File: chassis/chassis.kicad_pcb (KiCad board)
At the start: 2 copper layers, 157.5 x 43.2 mm, 84 parts, among them J1 RJ45_LED_Shielded, Q1 SiR422DP, Q2 Si7898DP, Q3 MMDT3906, T1 PoE_Transformer, T2 Pulse_Transformer, U1 TPS23754PWPR, U2 TCMT1107, U3 TCMT1107, U4 KSZ8081RND, U5 L78L33_SO8, U6 EFM32GG11B8xx

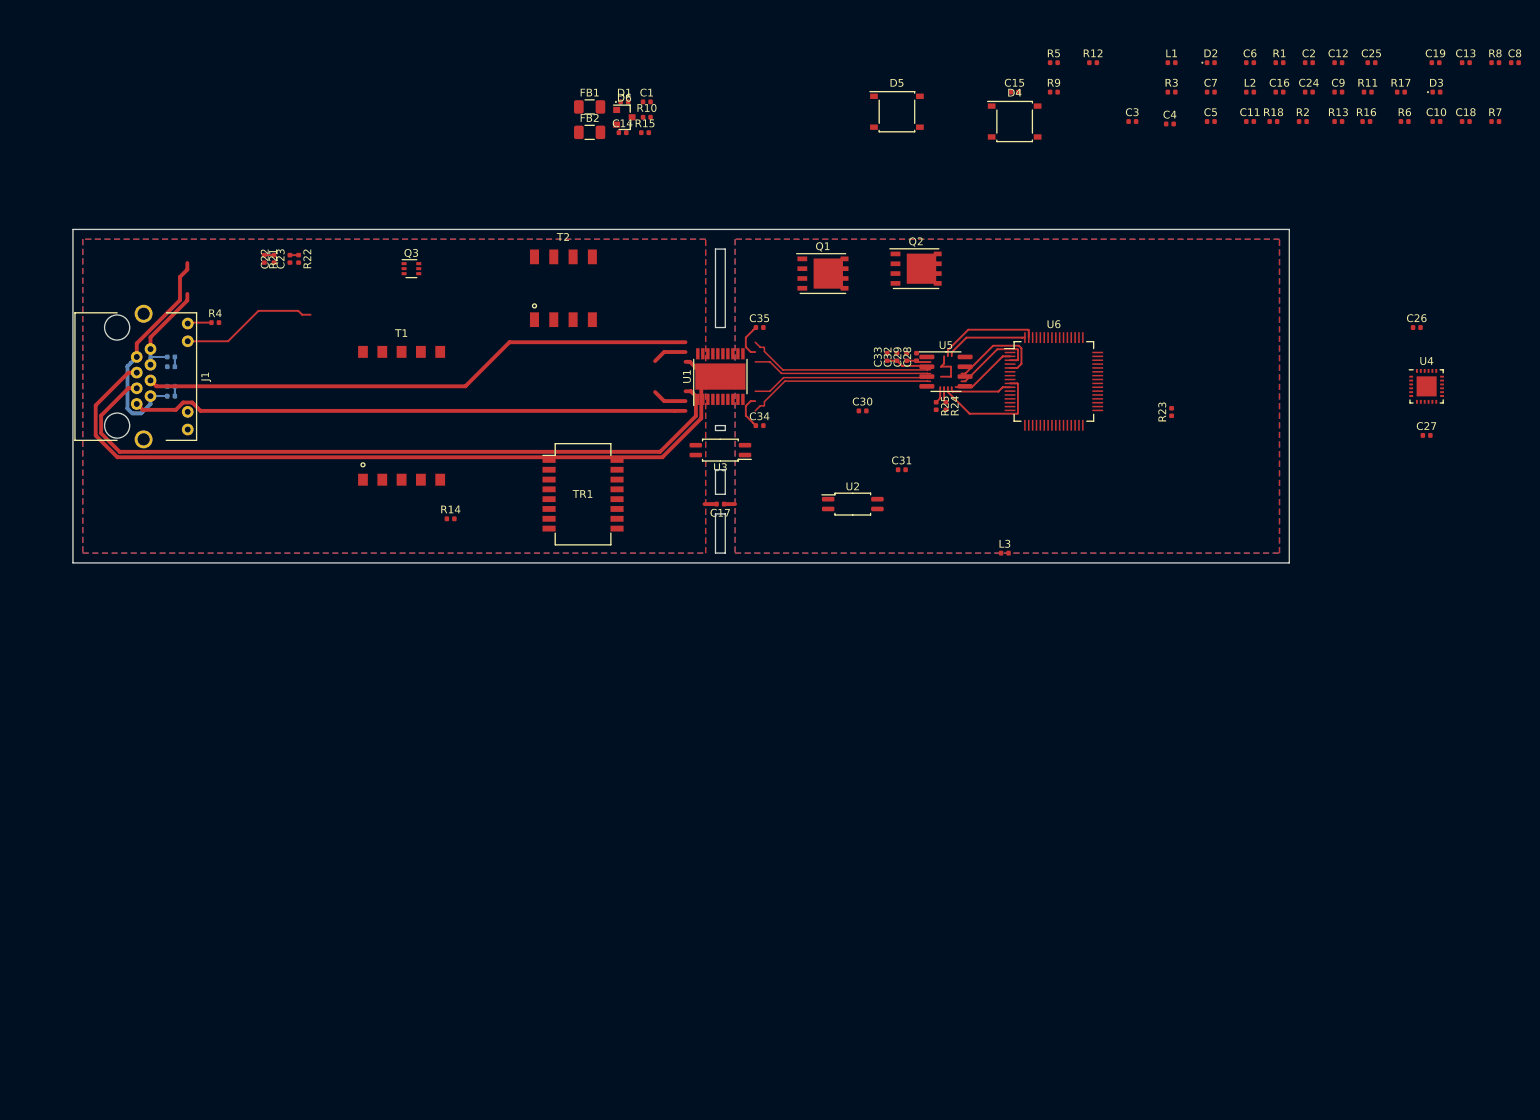
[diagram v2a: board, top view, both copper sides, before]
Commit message: hardware/*: finalize initial schematic and layout
This marks the initial revision of the board.
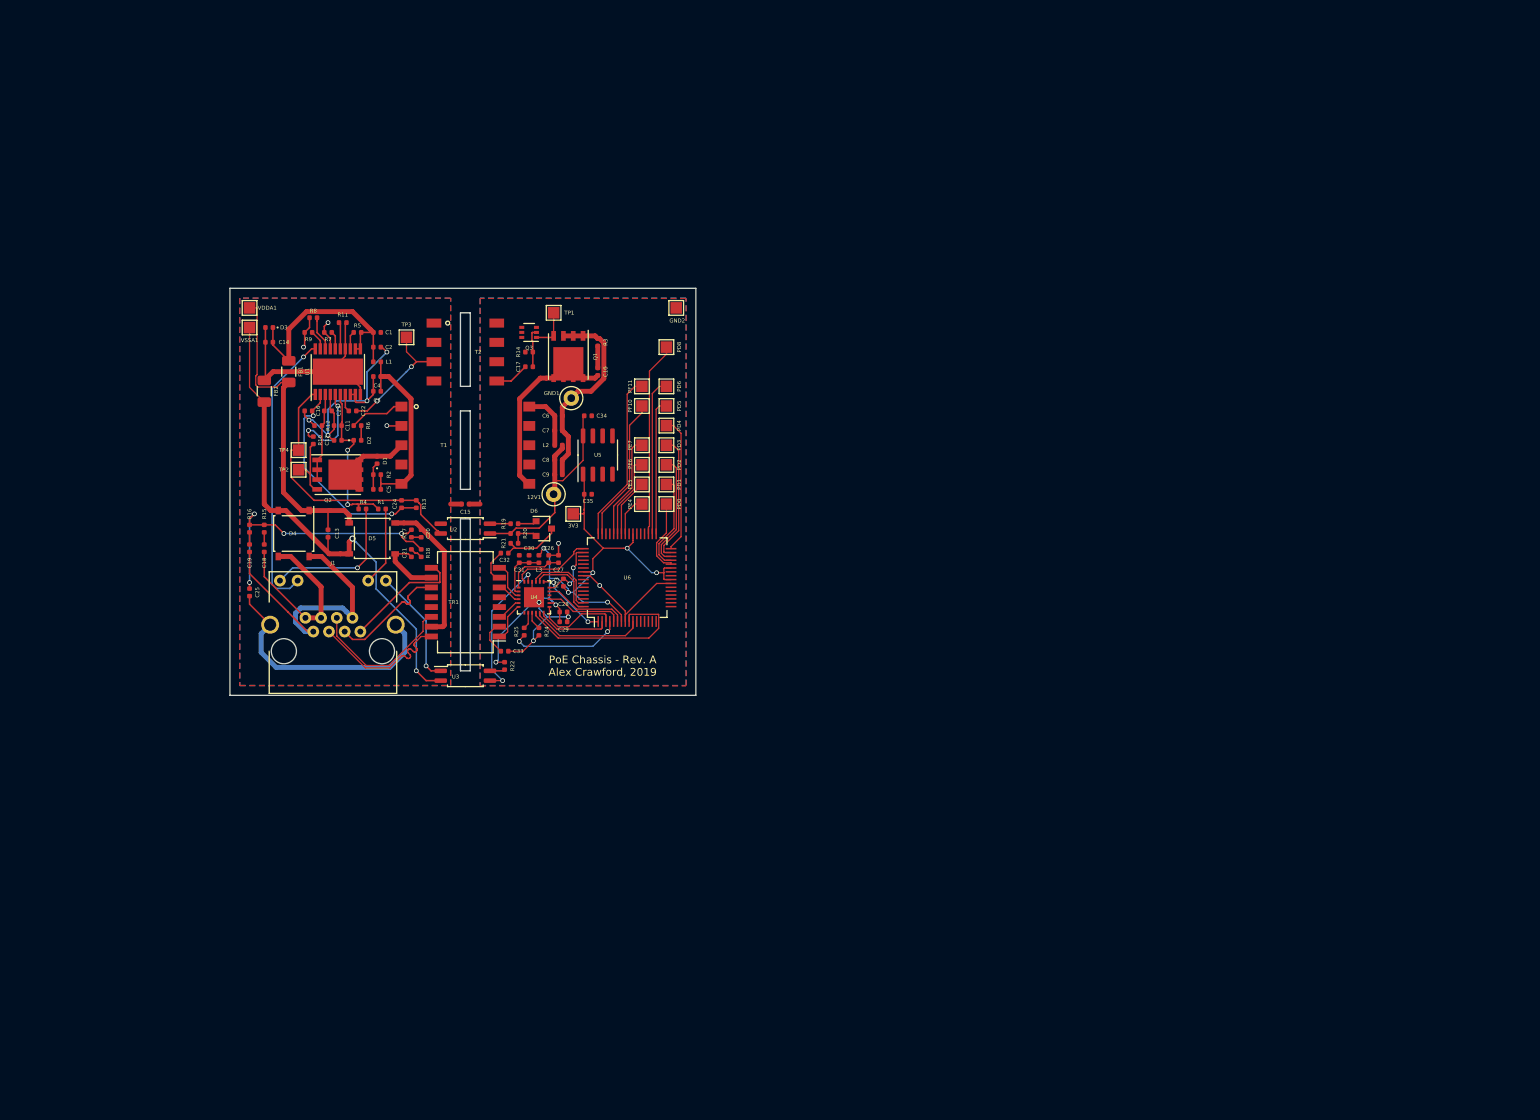
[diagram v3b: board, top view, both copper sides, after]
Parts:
- added 12V1: TestPoint, TestPoint:TestPoint_Loop_D1.80mm_Drill1.0mm_Beaded, F.Cu at (151.1, 97.8)
- added 3V3: TestPoint, TestPoint:TestPoint_Pad_1.5x1.5mm, F.Cu at (153.7, 100.3)
- added GND1: TestPoint, TestPoint:TestPoint_Loop_D1.80mm_Drill1.0mm_Beaded, F.Cu at (153.4, 85.3)
- added GND2: TestPoint, TestPoint:TestPoint_Pad_1.5x1.5mm, F.Cu at (167.0, 73.7)
- added PD0: TestPoint, TestPoint:TestPoint_Pad_1.5x1.5mm, F.Cu at (165.7, 99.1)
- added PD1: TestPoint, TestPoint:TestPoint_Pad_1.5x1.5mm, F.Cu at (165.7, 96.5)
- added PD2: TestPoint, TestPoint:TestPoint_Pad_1.5x1.5mm, F.Cu at (165.7, 94.0)
- added PD3: TestPoint, TestPoint:TestPoint_Pad_1.5x1.5mm, F.Cu at (165.7, 91.4)
- added PD4: TestPoint, TestPoint:TestPoint_Pad_1.5x1.5mm, F.Cu at (165.7, 88.9)
- added PD5: TestPoint, TestPoint:TestPoint_Pad_1.5x1.5mm, F.Cu at (165.7, 86.4)
- added PD6: TestPoint, TestPoint:TestPoint_Pad_1.5x1.5mm, F.Cu at (165.7, 83.8)
- added PD8: TestPoint, TestPoint:TestPoint_Pad_1.5x1.5mm, F.Cu at (165.7, 78.7)
- added PE4: TestPoint, TestPoint:TestPoint_Pad_1.5x1.5mm, F.Cu at (162.6, 99.1)
- added PE5: TestPoint, TestPoint:TestPoint_Pad_1.5x1.5mm, F.Cu at (162.6, 96.5)
- added PE6: TestPoint, TestPoint:TestPoint_Pad_1.5x1.5mm, F.Cu at (162.6, 94.0)
- added PE7: TestPoint, TestPoint:TestPoint_Pad_1.5x1.5mm, F.Cu at (162.6, 91.4)
- added PF10: TestPoint, TestPoint:TestPoint_Pad_1.5x1.5mm, F.Cu at (162.6, 86.4)
- added PF11: TestPoint, TestPoint:TestPoint_Pad_1.5x1.5mm, F.Cu at (162.6, 83.8)
- added TP1: TestPoint, TestPoint:TestPoint_Pad_1.5x1.5mm, F.Cu at (151.1, 74.3)
- added TP2: TestPoint, TestPoint:TestPoint_Pad_1.5x1.5mm, F.Cu at (118.1, 94.6)
- added TP3: TestPoint, TestPoint:TestPoint_Pad_1.5x1.5mm, F.Cu at (132.1, 77.5)
- added TP4: TestPoint, TestPoint:TestPoint_Pad_1.5x1.5mm, F.Cu at (118.1, 92.1)
- added VDDA1: TestPoint, TestPoint:TestPoint_Pad_1.5x1.5mm, F.Cu at (111.8, 73.7)
- added VSSA1: TestPoint, TestPoint:TestPoint_Pad_1.5x1.5mm, F.Cu at (111.8, 76.2)
- C20, C21, R19, R20: moved to F.Cu
- R1, R4: value 82 -> 1k2
- R13: value 10k -> 2k
- R14: value 2k -> 10k
- R21: value 560 -> 13k3
- R22: value 13k3 -> 100
- moved C19 165.9 mm to (111.8, 104.8), turned to 90 degrees
- moved C18 165.1 mm to (113.7, 104.8), turned to 90 degrees
- moved C25 160.6 mm to (111.8, 110.5), turned to 90 degrees
- moved C13 159.4 mm to (121.9, 102.9), turned to 270 degrees
- moved R8 156.6 mm to (120.0, 74.9), turned to 180 degrees
- moved D3 154.2 mm to (114.3, 76.2), turned to 180 degrees
- moved R16 153.9 mm to (111.8, 102.2), turned to 90 degrees
- moved R7 153.6 mm to (121.9, 76.8), turned to 180 degrees
- moved R6 141.2 mm to (125.7, 88.9), turned to 180 degrees
- moved R17 140.3 mm to (132.7, 102.9), turned to 90 degrees
- moved C12 138.5 mm to (123.2, 90.8), turned to 180 degrees
- moved R11 136.0 mm to (123.8, 75.6)
- moved C8 134.1 mm to (151.8, 93.3)
- moved C16 132.3 mm to (119.4, 87.0), turned to 180 degrees
- moved R1 129.8 mm to (128.9, 99.7), turned to 180 degrees
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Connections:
- net ETH_RX_M renamed ETH_RX-
- net ETH_RX_P renamed ETH_RX+
- net ETH_TX_M renamed ETH_TX-
- net ETH_TX_P renamed ETH_TX+
- D5 pad 3: Net-(C20-Pad1) -> Net-(C21-Pad1)
- D5 pad 4: Net-(C21-Pad1) -> Net-(C20-Pad1)
- J1 pad 1: Net-(J1-Pad1) -> /TX+
- J1 pad 11: POE_LED -> /T2P
- J1 pad 2: Net-(J1-Pad2) -> /TX-
- J1 pad 3: Net-(J1-Pad3) -> /RX+
- J1 pad 6: Net-(J1-Pad6) -> /RX-
- R1 pad 2: +3V3 -> /VC
- R13 pad 1: GNDD -> /VB
- R13 pad 2: Net-(C17-Pad1) -> /CTL
- R14 pad 1: /VB -> GNDD
- R14 pad 2: /CTL -> Net-(C17-Pad1)
- R21 pad 1: /VC -> GNDD
- R21 pad 2: Net-(R21-Pad2) -> Net-(D6-Pad2)
- R22 pad 1: GNDD -> +3V3
- R22 pad 2: Net-(D6-Pad2) -> Net-(R22-Pad2)
- R4 pad 2: +3V3 -> /VC
- TR1 pad 10: Net-(C20-Pad1) -> Net-(C21-Pad1)
- TR1 pad 11: Net-(J1-Pad3) -> /TX-
- TR1 pad 14: Net-(J1-Pad2) -> /RX-
- TR1 pad 15: Net-(C21-Pad1) -> Net-(C20-Pad1)
- TR1 pad 16: Net-(J1-Pad1) -> /RX+
- TR1 pad 2: ETH_TX_C -> ETH_RX_C
- TR1 pad 7: ETH_RX_C -> ETH_TX_C
- TR1 pad 9: Net-(J1-Pad6) -> /TX+
- U1 pad 10: VSSA -> Net-(C14-Pad2)
- U1 pad 21: VSSA -> Net-(C14-Pad2)
- U3 pad 1: POE_LED -> ETH_LED
- U3 pad 2: GNDD -> VSSA
- U3 pad 3: /T2P -> /ETH_LED0
- U3 pad 4: Net-(R21-Pad2) -> Net-(R22-Pad2)
- U4 pad 23: ETH_LED -> /ETH_LED0
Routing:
- net Net-(J1-Pad3): track 101.1 -> 0.00 mm
- net Net-(J1-Pad1): track 72.2 -> 0.00 mm
- net Net-(J1-Pad6): track 72.0 -> 0.00 mm
- net +3V3: track 7.71 -> 75.8 mm, vias 0 -> 8
- net VSSA: track 0.00 -> 65.9 mm, vias 0 -> 2
- net /CTL: track 92.5 -> 36.0 mm
- net GNDD: track 23.4 -> 71.8 mm, vias 0 -> 5
- net GNDA: track 0.00 -> 48.0 mm, vias 0 -> 7
- net VDDA: track 0.00 -> 43.4 mm
- net Net-(C19-Pad1): track 0.00 -> 37.4 mm
- net /T2P: track 0.00 -> 37.0 mm, vias 0 -> 1
- net Net-(C25-Pad2): track 0.00 -> 36.9 mm, vias 0 -> 4
- net Earth: track 0.00 -> 33.1 mm
- net Net-(C1-Pad1): track 0.00 -> 29.8 mm
- net Net-(C14-Pad2): track 0.00 -> 28.4 mm
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- added copper zone on B.Cu, net GNDD
- removed copper zone on B.Cu, net GND
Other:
- board size 157.5 x 43.2 mm -> 60.3 x 52.7 mm
- net class Default: clearance 0.2 -> 0.1524; trace_width 0.25 -> 0.1524; via_dia 0.8 -> 0.6096; via_drill 0.4 -> 0.4064
- net class Power: clearance 0.4 -> 0.3048; trace_width 0.5 -> 0.635; via_dia 0.8 -> 0.8128; via_drill 0.4 -> 0.508
- net class Signal added: clearance 0.2032, trace_width 0.2032, via_dia 0.7112, via_drill 0.4572
- rule trace_clearance: 0.2 -> 0.1524
- rule trace_min: 0.2 -> 0.1016
- rule via_min_size: 0.4 -> 0.1524
- board text added: "PoE Chassis - Rev. A Alex Crawford, 2019"

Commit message: chassis: update to KiCad 6
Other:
- net class Default removed
- net class Power removed
- net class Signal removed

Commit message: chassis: reset 3D models
KiCad 5 used KISYS3DMOD in the model paths, while KiCad 6 uses
KICAD6_3DMODEL_DIR instead. The metadata also got updated, which is nice.
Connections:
- C20 pad 1: Net-(C20-Pad1) -> Net-(C19-Pad1)
- D5 pad 4: Net-(C20-Pad1) -> Net-(C19-Pad1)
- TR1 pad 15: Net-(C20-Pad1) -> Net-(C19-Pad1)
- U4 pad 16: Net-(U4-Pad16) -> unconnected-(U4-Pad16)
- U4 pad 7: Net-(U4-Pad7) -> unconnected-(U4-Pad7)
- U5 pad 4: Net-(U5-Pad4) -> unconnected-(U5-Pad4)
- U5 pad 5: Net-(U5-Pad5) -> unconnected-(U5-Pad5)
- U6 pad 11: Net-(U6-Pad11) -> unconnected-(U6-Pad11)
- U6 pad 12: Net-(U6-Pad12) -> unconnected-(U6-Pad12)
- U6 pad 13: Net-(U6-Pad13) -> unconnected-(U6-Pad13)
- U6 pad 14: Net-(U6-Pad14) -> unconnected-(U6-Pad14)
- U6 pad 15: Net-(U6-Pad15) -> unconnected-(U6-Pad15)
- U6 pad 16: Net-(U6-Pad16) -> unconnected-(U6-Pad16)
- U6 pad 17: Net-(U6-Pad17) -> unconnected-(U6-Pad17)
- U6 pad 18: Net-(U6-Pad18) -> unconnected-(U6-Pad18)
- U6 pad 19: Net-(U6-Pad19) -> unconnected-(U6-Pad19)
- U6 pad 20: Net-(U6-Pad20) -> unconnected-(U6-Pad20)
- U6 pad 21: Net-(U6-Pad21) -> unconnected-(U6-Pad21)
- U6 pad 22: Net-(U6-Pad22) -> unconnected-(U6-Pad22)
- U6 pad 25: Net-(U6-Pad25) -> unconnected-(U6-Pad25)
- U6 pad 26: Net-(U6-Pad26) -> unconnected-(U6-Pad26)
- U6 pad 36: Net-(U6-Pad36) -> unconnected-(U6-Pad36)
- U6 pad 37: Net-(U6-Pad37) -> unconnected-(U6-Pad37)
- U6 pad 38: Net-(U6-Pad38) -> unconnected-(U6-Pad38)
- U6 pad 40: Net-(U6-Pad40) -> unconnected-(U6-Pad40)
- U6 pad 45: Net-(U6-Pad45) -> unconnected-(U6-Pad45)
- U6 pad 46: Net-(U6-Pad46) -> unconnected-(U6-Pad46)
- U6 pad 51: Net-(U6-Pad51) -> unconnected-(U6-Pad51)
- U6 pad 52: Net-(U6-Pad52) -> unconnected-(U6-Pad52)
- U6 pad 53: Net-(U6-Pad53) -> unconnected-(U6-Pad53)
- U6 pad 54: Net-(U6-Pad54) -> unconnected-(U6-Pad54)
- U6 pad 57: Net-(U6-Pad57) -> unconnected-(U6-Pad57)
- U6 pad 58: Net-(U6-Pad58) -> unconnected-(U6-Pad58)
- U6 pad 59: Net-(U6-Pad59) -> unconnected-(U6-Pad59)
- U6 pad 60: Net-(U6-Pad60) -> unconnected-(U6-Pad60)
- U6 pad 61: Net-(U6-Pad61) -> unconnected-(U6-Pad61)
- U6 pad 62: Net-(U6-Pad62) -> unconnected-(U6-Pad62)
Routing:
- net Net-(C19-Pad1): track 37.4 -> 56.7 mm
- net Net-(C20-Pad1): track 19.2 -> 0.00 mm
